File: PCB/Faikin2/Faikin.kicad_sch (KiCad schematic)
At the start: 25 parts, among them J1 1x5, J2 Shelly, J3 USB-PROG, Q1 BSS138PS, U2 ESP32-S3-MINI-1, U3 MD8942

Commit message: Cut out tidy
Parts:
- added Z1, Z2, Z3, Z4, Z5, Z6, Z7, Z8: Hidden, RevK:PCB-Join, symbol RevK:Hidden
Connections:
- new net: Z1.~, Z5.~
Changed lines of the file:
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@@
+    )
+  )
+  (symbol (lib_name "Hidden_1") (lib_id "RevK:Hidden") (at 259.08 175.26 90) (unit 1)
+    (in_bom yes) (on_board yes) (dnp no) (fields_autoplaced)
+    (property "Reference" "Z5" (at 259.08 173.9138 0)
+      (effects (font (size 1.27 1.27)) (justify left) hide)
+    )
+    (property "Value" "Hidden" (at 260.2921 173.9138 0)
+      (effects (font (size 1.27 1.27)) (justify left) hide)
+    )
+    (property "Footprint" "RevK:PCB-Join" (at 257.175 175.26 0)
+      (effects (font (size 1.27 1.27)) hide)
+    )
+    (property "Datasheet" "" (at 259.08 175.26 0)
+      (effects (font (size 1.27 1.27)) hide)
+    )
+    (property "Part No" "" (at 259.08 175.26 0)
+      (effects (font (size 1.27 1.27)) hide)
+    )
+    (property "Note" "" (at 259.08 175.26 0)
+      (effects (font (size 1.27 1.27)) hide)
+    )
+    (pin "~")
+    (instances
+      (project "Faikin"
+        (path "/46c350bb-7de4-4e81-aafd-4af55e37aab0"
+          (reference "Z5") (unit 1)
+        )
+      )
     )
   )
@@
         (path "/46c350bb-7de4-4e81-aafd-4af55e37aab0"
           (reference "#PWR09") (unit 1)
+        )
+      )
+    )
+  )
+  (symbol (lib_name "Hidden_1") (lib_id "RevK:Hidden") (at 265.43 175.26 90) (unit 1)
+    (in_bom yes) (on_board yes) (dnp no) (fields_autoplaced)
+    (property "Reference" "Z7" (at 265.43 173.9138 0)
+      (effects (font (size 1.27 1.27)) (justify left) hide)
+    )
+    (property "Value" "Hidden" (at 266.6421 173.9138 0)
+      (effects (font (size 1.27 1.27)) (justify left) hide)
+    )
+    (property "Footprint" "RevK:PCB-Join" (at 263.525 175.26 0)
+      (effects (font (size 1.27 1.27)) hide)
+    )
+    (property "Datasheet" "" (at 265.43 175.26 0)
+      (effects (font (size 1.27 1.27)) hide)
+    )
+    (property "Part No" "" (at 265.43 175.26 0)
+      (effects (font (size 1.27 1.27)) hide)
+    )
+    (property "Note" "" (at 265.43 175.26 0)
+      (effects (font (size 1.27 1.27)) hide)
+    )
+    (pin "~")
+    (instances
+      (project "Faikin"
+        (path "/46c350bb-7de4-4e81-aafd-4af55e37aab0"
+          (reference "Z7") (unit 1)
         )
       )
@@
     )
   )
+  (symbol (lib_name "Hidden_1") (lib_id "RevK:Hidden") (at 263.525 176.53 0) (unit 1)
+    (in_bom yes) (on_board yes) (dnp no) (fields_autoplaced)
+    (property "Reference" "Z4" (at 264.8712 176.53 0)
+      (effects (font (size 1.27 1.27)) (justify left) hide)
+    )
+    (property "Value" "Hidden" (at 264.8712 177.7421 0)
+      (effects (font (size 1.27 1.27)) (justify left) hide)
+    )
+    (property "Footprint" "RevK:PCB-Join" (at 263.525 174.625 0)
+      (effects (font (size 1.27 1.27)) hide)
+    )
+    (property "Datasheet" "" (at 263.525 176.53 0)
+      (effects (font (size 1.27 1.27)) hide)
+    )
+    (property "Part No" "" (at 263.525 176.53 0)
+      (effects (font (size 1.27 1.27)) hide)
+    )
+    (property "Note" "" (at 263.525 176.53 0)
+      (effects (font (size 1.27 1.27)) hide)
+    )
+    (pin "~")
+    (instances
+      (project "Faikin"
+        (path "/46c350bb-7de4-4e81-aafd-4af55e37aab0"
+          (reference "Z4") (unit 1)
+        )
+      )
+    )
+  )
   (symbol (lib_id "RevK:USB-PROG") (at 107.315 137.16 0) (unit 1)
     (in_bom yes) (on_board yes) (dnp no) (fields_autoplaced)
@@
     )
   )
+  (symbol (lib_name "Hidden_1") (lib_id "RevK:Hidden") (at 261.62 172.72 0) (unit 1)
+    (in_bom yes) (on_board yes) (dnp no) (fields_autoplaced)
+    (property "Reference" "Z1" (at 262.9662 172.72 0)
+      (effects (font (size 1.27 1.27)) (justify left) hide)
+    )
+    (property "Value" "Hidden" (at 262.9662 173.9321 0)
+      (effects (font (size 1.27 1.27)) (justify left) hide)
+    )
+    (property "Footprint" "RevK:PCB-Join" (at 261.62 170.815 0)
+      (effects (font (size 1.27 1.27)) hide)
+    )
+    (property "Datasheet" "" (at 261.62 172.72 0)
+      (effects (font (size 1.27 1.27)) hide)
+    )
+    (property "Part No" "" (at 261.62 172.72 0)
+      (effects (font (size 1.27 1.27)) hide)
+    )
+    (property "Note" "" (at 261.62 172.72 0)
+      (effects (font (size 1.27 1.27)) hide)
+    )
+    (pin "~")
+    (instances
+      (project "Faikin"
+        (path "/46c350bb-7de4-4e81-aafd-4af55e37aab0"
+          (reference "Z1") (unit 1)
+        )
+      )
+    )
+  )
   (symbol (lib_id "power:GND") (at 67.31 32.385 0) (unit 1)
     (in_bom yes) (on_board yes) (dnp no) (fields_autoplaced)
@@
         (path "/46c350bb-7de4-4e81-aafd-4af55e37aab0"
           (reference "#PWR011") (unit 1)
+        )
+      )
+    )
+  )
+  (symbol (lib_name "Hidden_1") (lib_id "RevK:Hidden") (at 259.08 173.355 90) (unit 1)
+    (in_bom yes) (on_board yes) (dnp no) (fields_autoplaced)
+    (property "Reference" "Z6" (at 259.08 172.0088 0)
+      (effects (font (size 1.27 1.27)) (justify left) hide)
+    )
+    (property "Value" "Hidden" (at 260.2921 172.0088 0)
+      (effects (font (size 1.27 1.27)) (justify left) hide)
+    )
+    (property "Footprint" "RevK:PCB-Join" (at 257.175 173.355 0)
+      (effects (font (size 1.27 1.27)) hide)
+    )
+    (property "Datasheet" "" (at 259.08 173.355 0)
+      (effects (font (size 1.27 1.27)) hide)
+    )
+    (property "Part No" "" (at 259.08 173.355 0)
+      (effects (font (size 1.27 1.27)) hide)
+    )
+    (property "Note" "" (at 259.08 173.355 0)
+      (effects (font (size 1.27 1.27)) hide)
+    )
+    (pin "~")
+    (instances
+      (project "Faikin"
+        (path "/46c350bb-7de4-4e81-aafd-4af55e37aab0"
+          (reference "Z6") (unit 1)
+        )
+      )
+    )
+  )
+  (symbol (lib_name "Hidden_1") (lib_id "RevK:Hidden") (at 261.62 176.53 0) (unit 1)
+    (in_bom yes) (on_board yes) (dnp no) (fields_autoplaced)
+    (property "Reference" "Z3" (at 262.9662 176.53 0)
+      (effects (font (size 1.27 1.27)) (justify left) hide)
+    )
+    (property "Value" "Hidden" (at 262.9662 177.7421 0)
+      (effects (font (size 1.27 1.27)) (justify left) hide)
+    )
+    (property "Footprint" "RevK:PCB-Join" (at 261.62 174.625 0)
+      (effects (font (size 1.27 1.27)) hide)
+    )
+    (property "Datasheet" "" (at 261.62 176.53 0)
+      (effects (font (size 1.27 1.27)) hide)
+    )
+    (property "Part No" "" (at 261.62 176.53 0)
+      (effects (font (size 1.27 1.27)) hide)
+    )
+    (property "Note" "" (at 261.62 176.53 0)
+      (effects (font (size 1.27 1.27)) hide)
+    )
+    (pin "~")
+    (instances
+      (project "Faikin"
+        (path "/46c350bb-7de4-4e81-aafd-4af55e37aab0"
+          (reference "Z3") (unit 1)
         )
       )
@@
     )
   )
+  (symbol (lib_name "Hidden_1") (lib_id "RevK:Hidden") (at 263.525 172.72 0) (unit 1)
+    (in_bom yes) (on_board yes) (dnp no) (fields_autoplaced)
+    (property "Reference" "Z2" (at 264.8712 172.72 0)
+      (effects (font (size 1.27 1.27)) (justify left) hide)
+    )
+    (property "Value" "Hidden" (at 264.8712 173.9321 0)
+      (effects (font (size 1.27 1.27)) (justify left) hide)
+    )
+    (property "Footprint" "RevK:PCB-Join" (at 263.525 170.815 0)
+      (effects (font (size 1.27 1.27)) hide)
+    )
+    (property "Datasheet" "" (at 263.525 172.72 0)
+      (effects (font (size 1.27 1.27)) hide)
+    )
+    (property "Part No" "" (at 263.525 172.72 0)
+      (effects (font (size 1.27 1.27)) hide)
+    )
+    (property "Note" "" (at 263.525 172.72 0)
+      (effects (font (size 1.27 1.27)) hide)
+    )
+    (pin "~")
+    (instances
+      (project "Faikin"
+        (path "/46c350bb-7de4-4e81-aafd-4af55e37aab0"
+          (reference "Z2") (unit 1)
+        )
+      )
+    )
+  )
   (symbol (lib_id "power:+3.3V") (at 67.31 24.765 0) (unit 1)
     (in_bom yes) (on_board yes) (dnp no) (fields_autoplaced)
@@
         )
       )
+    )
+  )
+  (symbol (lib_name "Hidden_1") (lib_id "RevK:Hidden") (at 265.43 173.355 90) (unit 1)
+    (in_bom yes) (on_board yes) (dnp no) (fields_autoplaced)
+    (property "Reference" "Z8" (at 265.43 172.0088 0)
+      (effects (font (size 1.27 1.27)) (justify left) hide)
+    )
+    (property "Value" "Hidden" (at 266.6421 172.0088 0)
+      (effects (font (size 1.27 1.27)) (justify left) hide)
+    )
+    (property "Footprint" "RevK:PCB-Join" (at 263.525 173.355 0)
+      (effects (font (size 1.27 1.27)) hide)
+    )
+    (property "Datasheet" "" (at 265.43 173.355 0)
+      (effects (font (size 1.27 1.27)) hide)
+    )
+    (property "Part No" "" (at 265.43 173.355 0)
+      (effects (font (size 1.27 1.27)) hide)
+    )
+    (property "Note" "" (at 265.43 173.355 0)
+      (effects (font (size 1.27 1.27)) hide)
+    )
+    (pin "~")
+    (instances
+      (project "Faikin"
+        (path "/46c350bb-7de4-4e81-aafd-4af55e37aab0"
+          (reference "Z8") (unit 1)
+        )
+      )

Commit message: Snap out
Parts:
- Z1, Z2, Z3, Z4, Z5, Z6, Z7, Z8: footprint RevK:PCB-Join -> RevK:PCB-Join1
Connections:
- net at Z1.~: no longer Z5.~

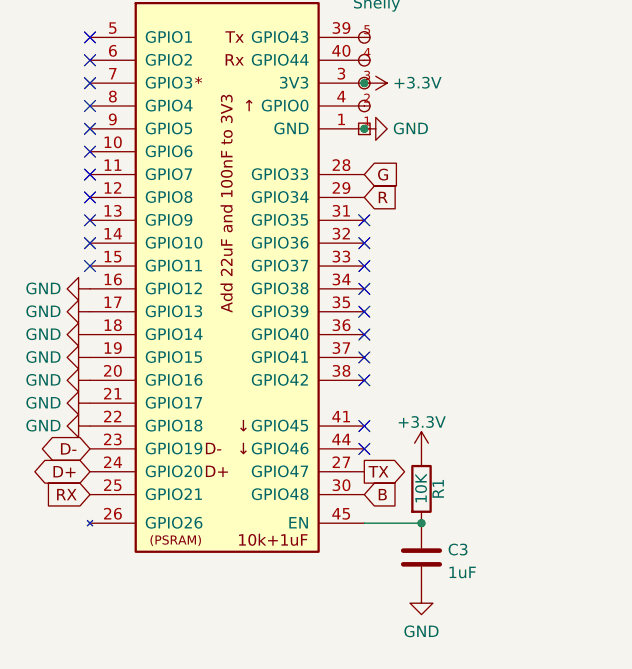
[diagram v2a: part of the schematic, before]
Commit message: Further rework of tx/rx (and change of GPIO)
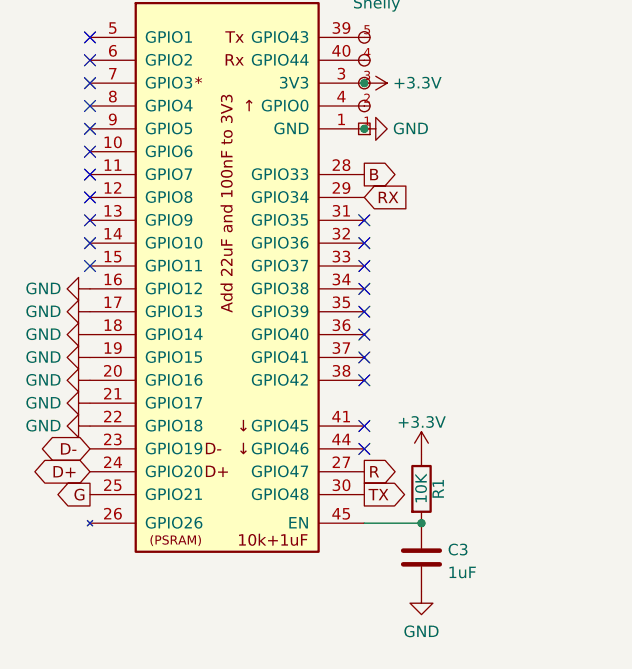
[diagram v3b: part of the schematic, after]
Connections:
- net B: now also U2.28 (GPIO33); no longer U2.30 (GPIO48)
- net G: now also U2.25 (GPIO21); no longer U2.28 (GPIO33)
- net R: now also U2.27 (GPIO47); no longer U2.29 (GPIO34)
- net RX: now also U2.29 (GPIO34); no longer U2.25 (GPIO21)
- net TX: now also U2.30 (GPIO48); no longer U2.27 (GPIO47)
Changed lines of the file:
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@@
     )
   )
-  (global_label "G" (shape input) (at 79.375 63.5 0) (fields_autoplaced)
-    (effects (font (size 1.27 1.27)) (justify left))
-    (property "Intersheetrefs" "${INTERSHEET_REFS}" (at 182.245 163.83 0)
-      (effects (font (size 1.27 1.27)) hide)
+  (global_label "G" (shape output) (at 48.895 99.06 180) (fields_autoplaced)
+    (effects (font (size 1.27 1.27)) (justify right))
+    (property "Intersheetrefs" "${INTERSHEET_REFS}" (at 45.294 99.06 0)
+      (effects (font (size 1.27 1.27)) (justify right) hide)
     )
   )
-  (global_label "R" (shape input) (at 79.375 66.04 0) (fields_autoplaced)
+  (global_label "R" (shape output) (at 79.375 96.52 0) (fields_autoplaced)
     (effects (font (size 1.27 1.27)) (justify left))
-    (property "Intersheetrefs" "${INTERSHEET_REFS}" (at 82.8966 66.04 0)
+    (property "Intersheetrefs" "${INTERSHEET_REFS}" (at 82.976 96.52 0)
       (effects (font (size 1.27 1.27)) (justify left) hide)
     )
@@
     )
   )
-  (global_label "TX" (shape output) (at 79.375 96.52 0) (fields_autoplaced)
+  (global_label "TX" (shape output) (at 79.375 99.06 0) (fields_autoplaced)
     (effects (font (size 1.27 1.27)) (justify left))
-    (property "Intersheetrefs" "${INTERSHEET_REFS}" (at 83.8763 96.4406 0)
+    (property "Intersheetrefs" "${INTERSHEET_REFS}" (at 83.8763 98.9806 0)
       (effects (font (size 1.27 1.27)) (justify left) hide)
     )
@@
     )
   )
-  (global_label "RX" (shape input) (at 48.895 99.06 180) (fields_autoplaced)
-    (effects (font (size 1.27 1.27)) (justify right))
-    (property "Intersheetrefs" "${INTERSHEET_REFS}" (at 44.1639 99.06 0)
-      (effects (font (size 1.27 1.27)) (justify right) hide)
+  (global_label "RX" (shape input) (at 79.375 66.04 0) (fields_autoplaced)
+    (effects (font (size 1.27 1.27)) (justify left))
+    (property "Intersheetrefs" "${INTERSHEET_REFS}" (at 84.1855 66.04 0)
+      (effects (font (size 1.27 1.27)) (justify left) hide)
     )
   )
@@
     )
   )
-  (global_label "B" (shape input) (at 79.375 99.06 0) (fields_autoplaced)
+  (global_label "B" (shape output) (at 79.375 63.5 0) (fields_autoplaced)
     (effects (font (size 1.27 1.27)) (justify left))
-    (property "Intersheetrefs" "${INTERSHEET_REFS}" (at 82.8966 99.06 0)
+    (property "Intersheetrefs" "${INTERSHEET_REFS}" (at 82.976 63.5 0)
       (effects (font (size 1.27 1.27)) (justify left) hide)
     )

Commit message: Bigger cap
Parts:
- C2: footprint RevK:C_0402 -> RevK:C_0603
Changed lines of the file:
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@@
       (effects (font (size 1.27 1.27)) (justify left))
     )
-    (property "Footprint" "RevK:C_0402" (at 68.2752 32.385 0)
+    (property "Footprint" "RevK:C_0603" (at 68.2752 32.385 0)
       (effects (font (size 1.27 1.27)) hide)
     )

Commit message: Even more cautious
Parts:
- Z1, Z2, Z3, Z4, Z5, Z6, Z7, Z8: now left out of the parts list
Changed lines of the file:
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@@
   )
   (symbol (lib_name "Hidden_1") (lib_id "RevK:Hidden") (at 260.985 172.72 0) (unit 1)
-    (in_bom yes) (on_board yes) (dnp no) (fields_autoplaced)
+    (in_bom no) (on_board yes) (dnp no) (fields_autoplaced)
     (property "Reference" "Z1" (at 262.3312 172.72 0)
       (effects (font (size 1.27 1.27)) (justify left) hide)
@@
   )
   (symbol (lib_name "Hidden_1") (lib_id "RevK:Hidden") (at 259.08 173.355 90) (unit 1)
-    (in_bom yes) (on_board yes) (dnp no) (fields_autoplaced)
+    (in_bom no) (on_board yes) (dnp no) (fields_autoplaced)
     (property "Reference" "Z6" (at 259.08 172.0088 0)
       (effects (font (size 1.27 1.27)) (justify left) hide)
@@
   )
   (symbol (lib_name "Hidden_1") (lib_id "RevK:Hidden") (at 263.525 172.72 0) (unit 1)
-    (in_bom yes) (on_board yes) (dnp no) (fields_autoplaced)
+    (in_bom no) (on_board yes) (dnp no) (fields_autoplaced)
     (property "Reference" "Z2" (at 264.8712 172.72 0)
       (effects (font (size 1.27 1.27)) (justify left) hide)
@@
   )
   (symbol (lib_name "Hidden_1") (lib_id "RevK:Hidden") (at 265.43 175.895 90) (unit 1)
-    (in_bom yes) (on_board yes) (dnp no) (fields_autoplaced)
+    (in_bom no) (on_board yes) (dnp no) (fields_autoplaced)
     (property "Reference" "Z8" (at 265.43 174.5488 0)
       (effects (font (size 1.27 1.27)) (justify left) hide)
@@
   )
   (symbol (lib_name "Hidden_1") (lib_id "RevK:Hidden") (at 259.08 175.895 90) (unit 1)
-    (in_bom yes) (on_board yes) (dnp no) (fields_autoplaced)
+    (in_bom no) (on_board yes) (dnp no) (fields_autoplaced)
     (property "Reference" "Z5" (at 259.08 174.5488 0)
       (effects (font (size 1.27 1.27)) (justify left) hide)
@@
   )
   (symbol (lib_name "Hidden_1") (lib_id "RevK:Hidden") (at 263.525 176.53 0) (unit 1)
-    (in_bom yes) (on_board yes) (dnp no) (fields_autoplaced)
+    (in_bom no) (on_board yes) (dnp no) (fields_autoplaced)
     (property "Reference" "Z4" (at 264.8712 176.53 0)
       (effects (font (size 1.27 1.27)) (justify left) hide)
@@
   )
   (symbol (lib_name "Hidden_1") (lib_id "RevK:Hidden") (at 265.43 173.355 90) (unit 1)
-    (in_bom yes) (on_board yes) (dnp no) (fields_autoplaced)
+    (in_bom no) (on_board yes) (dnp no) (fields_autoplaced)
     (property "Reference" "Z7" (at 265.43 172.0088 0)
       (effects (font (size 1.27 1.27)) (justify left) hide)
@@
   )
   (symbol (lib_name "Hidden_1") (lib_id "RevK:Hidden") (at 260.985 176.53 0) (unit 1)
-    (in_bom yes) (on_board yes) (dnp no) (fields_autoplaced)
+    (in_bom no) (on_board yes) (dnp no) (fields_autoplaced)
     (property "Reference" "Z3" (at 262.3312 176.53 0)
       (effects (font (size 1.27 1.27)) (justify left) hide)

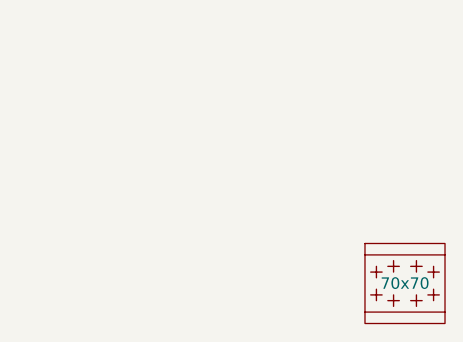
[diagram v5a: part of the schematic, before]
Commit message: Better cut out
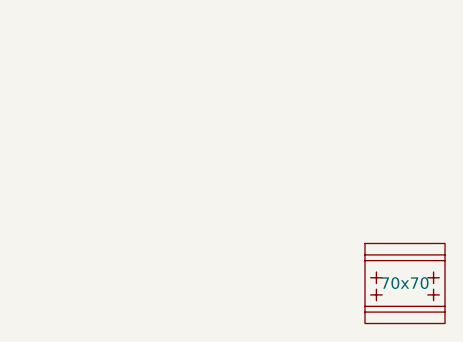
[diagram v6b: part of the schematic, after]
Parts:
- removed Z5, Z6, Z7, Z8: Hidden, RevK:PCB-Join1, symbol RevK:Hidden
- added V3, V4: ~, RevK:VCUT70, symbol RevK:VCUT
